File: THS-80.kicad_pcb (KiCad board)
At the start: 4 copper layers, 102.6 x 51.4 mm, 93 parts, among them J1 RC80 Bus, J2 CTC Header, J3 AVR-JTAG-10, J4 IDE, J5 PIO Header, J6 Port A, J7 Port B, J8 USB_B_Micro, Q1 IRLML6402, SW1 Reset, U1 DS1813R-5+T&R, U10 Z84C2010AEG, U11 74HCT273, U12 MAX40200AUK, U3 CPU -Z84C0020AEG, U4 CTC - Z84C3010AEG, U5 CPLD - EPM7032STC44, U6 SRAM - IS62C5128BL-45TLI, U7 74HCT2G04, U8 SST39SF040, U9 SIO/3 - Z84C4310AEG, X1 CFPS-72 50mhz

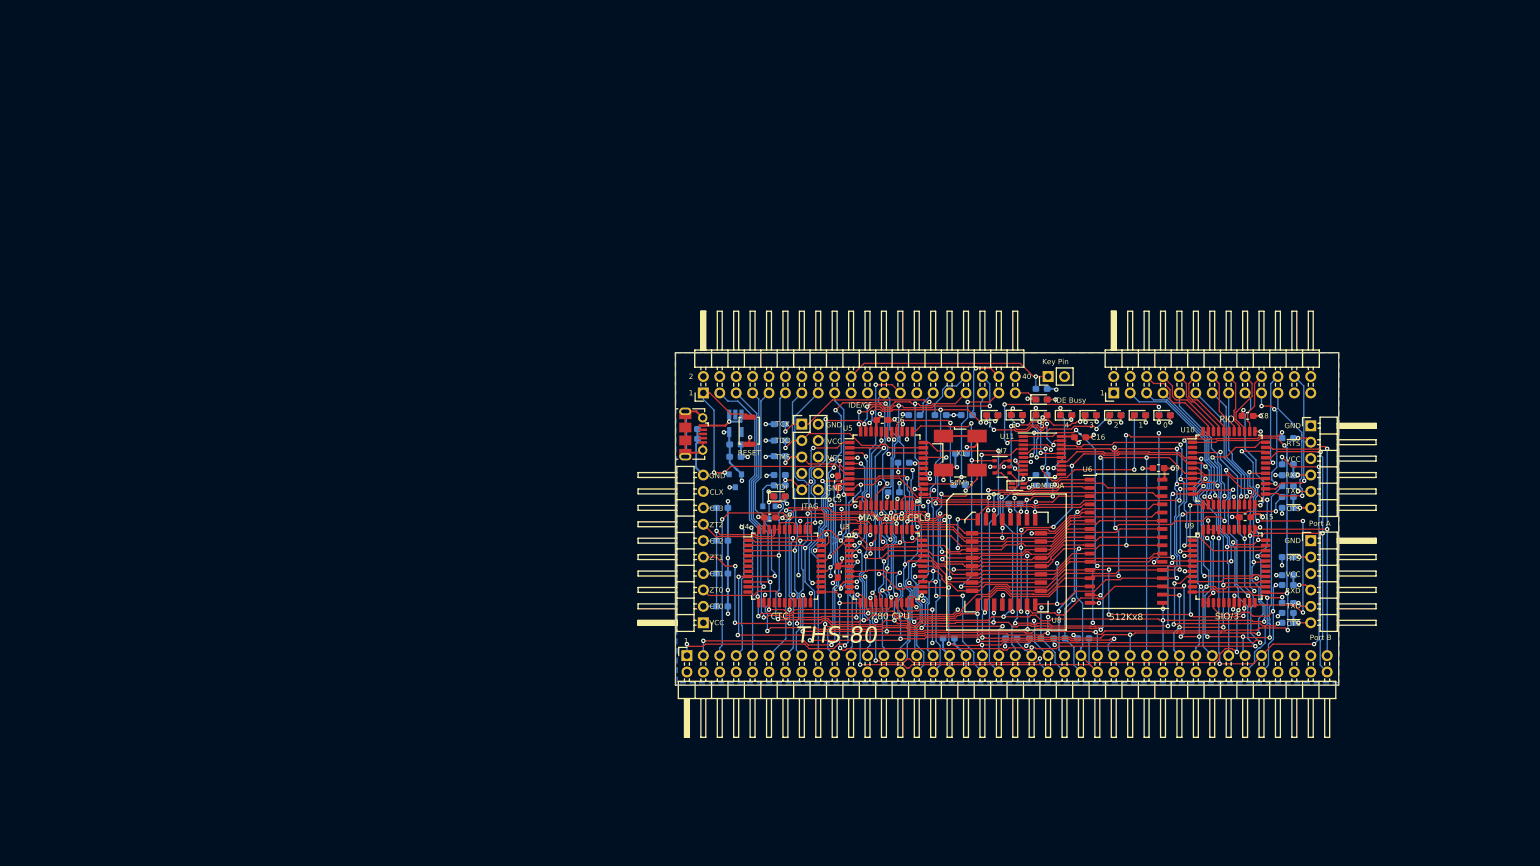
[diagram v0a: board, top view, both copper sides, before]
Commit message: connected sheet pins to bus
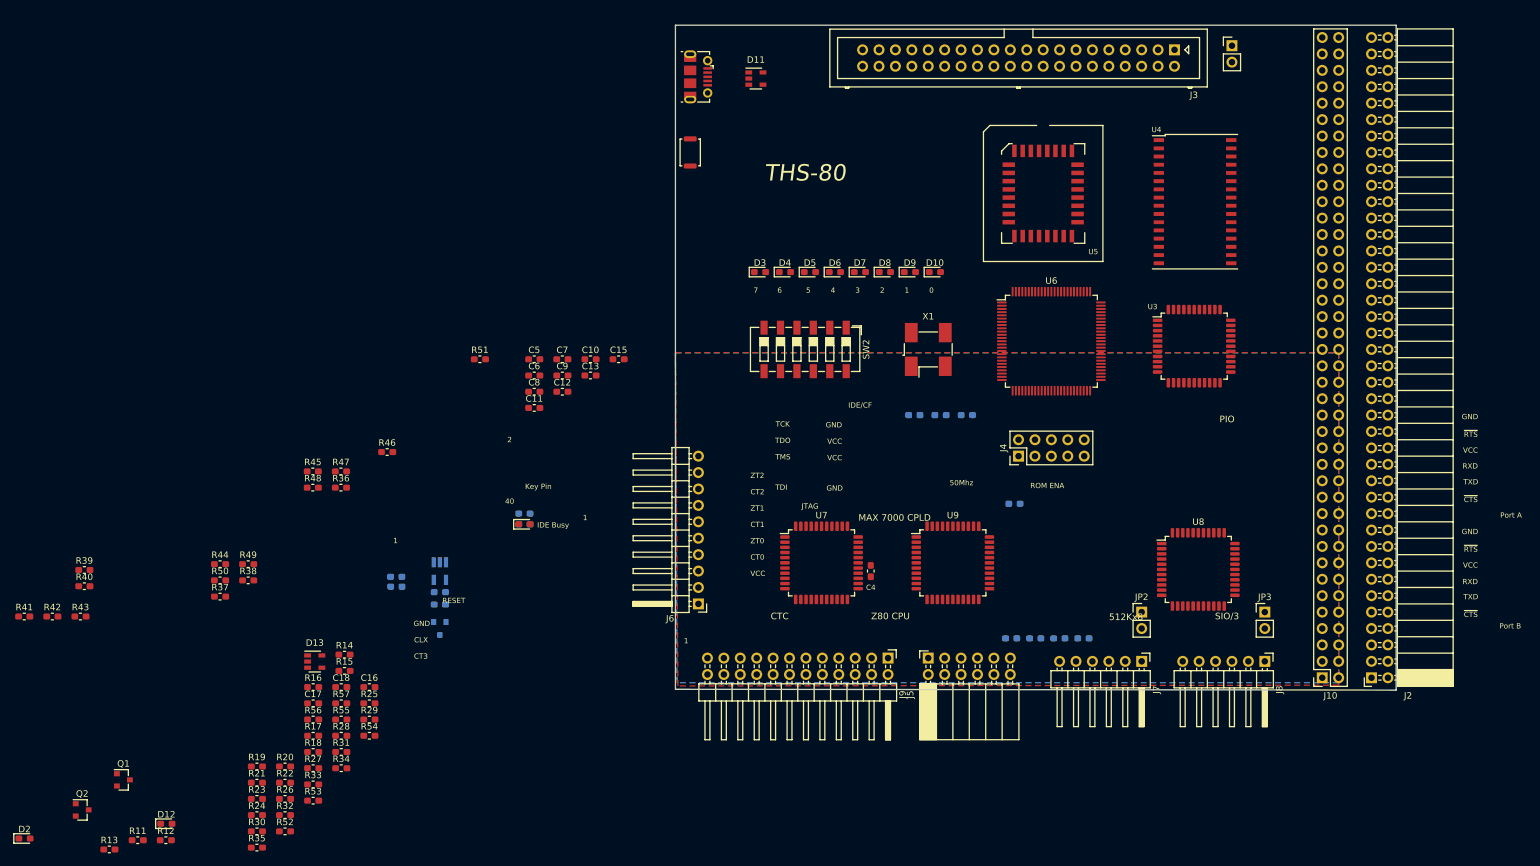
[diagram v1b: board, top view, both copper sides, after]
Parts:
- removed the C2 at (116.5, 107.3)
- removed the C3 at (137.2, 98.8)
- removed the C4 at (135.6, 103.4)
- removed the D1 at (117.9, 104.0)
- removed the J2 at (106.2, 123.6)
- removed the J3 at (121.4, 92.8)
- removed the R10 at (118.0, 92.8)
- removed the R3 at (145.8, 102.2)
- removed the R6 at (109.1, 116.0)
- removed the R7 at (109.1, 110.9)
- removed the R8 at (109.1, 105.8)
- removed the R9 at (109.1, 121.0)
- removed U10: Z84C2010AEG, Package_QFP:LQFP-44_10x10mm_P0.8mm
- removed U11: 74HCT273, Package_SO:TSSOP-20_4.4x6.5mm_P0.65mm
- removed the U4 at (118.7, 114.8)
- removed the U5 at (134.5, 99.7)
- added C10: 100nF, Capacitor_SMD:C_0603_1608Metric_Pad1.05x0.95mm_HandSolder, F.Cu at (88.7, 82.8)
- added C12: 100nF, Capacitor_SMD:C_0603_1608Metric_Pad1.05x0.95mm_HandSolder, F.Cu at (84.4, 87.8)
- added C13: 100nF, Capacitor_SMD:C_0603_1608Metric_Pad1.05x0.95mm_HandSolder, F.Cu at (88.7, 85.3)
- added C17: 100nF, Capacitor_SMD:C_0603_1608Metric_Pad1.05x0.95mm_HandSolder, F.Cu at (45.8, 136.0)
- added C18: 100nF, Capacitor_SMD:C_0603_1608Metric_Pad1.05x0.95mm_HandSolder, F.Cu at (50.1, 133.5)
- added D12: Green, LED_SMD:LED_0603_1608Metric_Pad1.05x0.95mm_HandSolder, F.Cu at (23.1, 154.7)
- added D13: SP0504BAHT, Package_TO_SOT_SMD:SOT-23-5, F.Cu at (46.0, 129.6)
- added D2: Green, LED_SMD:LED_0603_1608Metric_Pad1.05x0.95mm_HandSolder, F.Cu at (1.15, 156.9)
- added J10: RC80 Bus, Connector_PinSocket_2.54mm:PinSocket_2x40_P2.54mm_Vertical, F.Cu at (201.9, 132.1)
- added J4: JTAG, Connector_PinHeader_2.54mm:PinHeader_2x05_P2.54mm_Vertical, F.Cu at (154.9, 97.8)
- added J8: Port A, Connector_PinHeader_2.54mm:PinHeader_1x06_P2.54mm_Horizontal, F.Cu at (193.0, 129.5)
- added J9: PIO Header, Connector_PinHeader_2.54mm:PinHeader_2x12_P2.54mm_Horizontal, F.Cu at (134.7, 129.0)
- added JP2: 5V, Connector_PinHeader_2.54mm:PinHeader_1x02_P2.54mm_Vertical, F.Cu at (174.0, 121.9)
- added JP3: 5V, Connector_PinHeader_2.54mm:PinHeader_1x02_P2.54mm_Vertical, F.Cu at (193.0, 121.9)
- added Q2: IRLML6402, Package_TO_SOT_SMD:SOT-23, F.Cu at (10.1, 152.5)
- added R11: 100R, Resistor_SMD:R_0603_1608Metric_Pad1.05x0.95mm_HandSolder, F.Cu at (18.7, 157.2)
- added R16: 10K, Resistor_SMD:R_0603_1608Metric_Pad1.05x0.95mm_HandSolder, F.Cu at (45.8, 133.5)
- added R18: 200R, Resistor_SMD:R_0603_1608Metric_Pad1.05x0.95mm_HandSolder, F.Cu at (45.8, 143.6)
- added R21: 200R, Resistor_SMD:R_0603_1608Metric_Pad1.05x0.95mm_HandSolder, F.Cu at (37.1, 148.3)
- added R22: 680R, Resistor_SMD:R_0603_1608Metric_Pad1.05x0.95mm_HandSolder, F.Cu at (41.5, 148.3)
- added R43: 2K2, Resistor_SMD:R_0603_1608Metric_Pad1.05x0.95mm_HandSolder, F.Cu at (9.80, 122.6)
- added R44: 2K2, Resistor_SMD:R_0603_1608Metric_Pad1.05x0.95mm_HandSolder, F.Cu at (31.4, 114.5)
- added R45: 2K2, Resistor_SMD:R_0603_1608Metric_Pad1.05x0.95mm_HandSolder, F.Cu at (45.8, 100.2)
- added R46: 2K2, Resistor_SMD:R_0603_1608Metric_Pad1.05x0.95mm_HandSolder, F.Cu at (57.2, 97.2)
- added R47: 2K2, Resistor_SMD:R_0603_1608Metric_Pad1.05x0.95mm_HandSolder, F.Cu at (50.1, 100.2)
- added R48: 100K, Resistor_SMD:R_0603_1608Metric_Pad1.05x0.95mm_HandSolder, F.Cu at (45.8, 102.7)
- added R49: 100K, Resistor_SMD:R_0603_1608Metric_Pad1.05x0.95mm_HandSolder, F.Cu at (35.8, 114.5)
- added R50: 100K, Resistor_SMD:R_0603_1608Metric_Pad1.05x0.95mm_HandSolder, F.Cu at (31.4, 117.0)
- added R51: 100K, Resistor_SMD:R_0603_1608Metric_Pad1.05x0.95mm_HandSolder, F.Cu at (71.6, 82.8)
- added R52: 10K, Resistor_SMD:R_0603_1608Metric_Pad1.05x0.95mm_HandSolder, F.Cu at (41.5, 155.8)
- added R53: 10K, Resistor_SMD:R_0603_1608Metric_Pad1.05x0.95mm_HandSolder, F.Cu at (45.8, 151.1)
- added R54: 10K, Resistor_SMD:R_0603_1608Metric_Pad1.05x0.95mm_HandSolder, F.Cu at (54.5, 141.1)
- added R55: 10K, Resistor_SMD:R_0603_1608Metric_Pad1.05x0.95mm_HandSolder, F.Cu at (50.1, 138.5)
- added R56: 10K, Resistor_SMD:R_0603_1608Metric_Pad1.05x0.95mm_HandSolder, F.Cu at (45.8, 138.5)
- added R57: 10K, Resistor_SMD:R_0603_1608Metric_Pad1.05x0.95mm_HandSolder, F.Cu at (50.1, 136.0)
- added SW2: SW_DIP_x06, Button_Switch_SMD:SW_DIP_SPSTx06_Slide_6.7x16.8mm_W6.73mm_P2.54mm_LowProfile_JPin, F.Cu at (121.9, 81.3)
- added U6: EPM7064STC100, Package_QFP:TQFP-100_14x14mm_P0.5mm, F.Cu at (160.0, 80.0)
- added U8: SIO/3 - Z84C4310AEG, Package_QFP:LQFP-44_10x10mm_P0.8mm, F.Cu at (182.8, 115.3)
- C11, Q1, R15, R17, R23, R24, R25, R26, R27, R28, R29: moved to F.Cu
- C16: value 100nF -> 2.2uF
- C7: value 2.2uF -> 100nF; moved to F.Cu
- D11: value Green -> SP0504BAHT; footprint LED_SMD:LED_0603_1608Metric_Pad1.05x0.95mm_HandSolder -> Package_TO_SOT_SMD:SOT-23-5
- D3: value Red/Green -> Green; footprint LED_SMD:LED_2C_0603_1608Metric_Pad1.05x0.95mm_HandSolder -> LED_SMD:LED_0603_1608Metric_Pad1.05x0.95mm_HandSolder
- J2: renamed from J1; footprint Connector_PinHeader_2.54mm:PinHeader_2x40_Top_Bottom_P2.54mm_Horizontal -> Connector_PinSocket_2.54mm:PinSocket_2x40_P2.54mm_Horizontal
- J3: renamed from J4; footprint Connector_PinHeader_2.54mm:PinHeader_2x20_P2.54mm_Horizontal -> Connector_Multicomp:Multicomp_MC9A12-4034_2x20_P2.54mm_Vertical
- J5: value PIO Header -> PMOD; footprint Connector_PinHeader_2.54mm:PinHeader_2x13_P2.54mm_Horizontal -> Connector_PinSocket_2.54mm:PinSocket_2x06_P2.54mm_Horizontal
- J6: value Port A -> CTC Header; footprint Connector_PinHeader_2.54mm:PinHeader_1x06_P2.54mm_Horizontal -> Connector_PinHeader_2.54mm:PinHeader_1x10_P2.54mm_Horizontal
- JP1: value Jumper_NC_Small -> Keypin
- R12: value 10K -> 1K; moved to F.Cu
- R13: value 100R -> 10K; moved to F.Cu
- R14: value 10K -> 100R; moved to F.Cu
- R19, R20: value 680R -> 200R; moved to F.Cu
- R30: value 680R -> 100R; moved to F.Cu
- R31: value 2K2 -> 360R; moved to F.Cu
- R32, R33, R34, R35: value 2K2 -> 200R; moved to F.Cu
- R36, R37, R38: value 2K2 -> 10K; moved to F.Cu
- R39: value 100K -> 10K; moved to F.Cu
- R40, R41, R42: value 100K -> 2K2; moved to F.Cu
- U7: value 74HCT2G04 -> CTC - Z84C3010AEG; footprint Package_SO:TSOP-6_1.65x3.05mm_P0.95mm -> Package_QFP:LQFP-44_10x10mm_P0.8mm
- U9: value SIO/3 - Z84C4310AEG -> Z84C2010AEG
- moved R41 196.2 mm to (1.10, 122.6), turned to 0 degrees
- moved R42 191.1 mm to (5.45, 122.6), turned to 0 degrees
- moved R39 186.8 mm to (10.4, 115.4)
- moved R40 186.2 mm to (10.4, 117.9)
- moved R35 165.7 mm to (37.1, 158.4), turned to 0 degrees
- moved R37 165.2 mm to (31.4, 119.5), turned to 0 degrees
- moved R32 164.4 mm to (41.5, 153.3), turned to 0 degrees
- moved R38 161.0 mm to (35.8, 117.0), turned to 0 degrees
- moved R33 157.7 mm to (45.8, 148.6), turned to 0 degrees
- moved R31 154.3 mm to (50.1, 143.6), turned to 0 degrees
- moved R23 152.5 mm to (37.1, 150.8)
- moved R34 152.3 mm to (50.1, 146.1), turned to 0 degrees
- moved R24 150.0 mm to (37.1, 153.3)
- moved R36 147.3 mm to (50.1, 102.7), turned to 0 degrees
- moved R26 138.1 mm to (41.5, 150.8)
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- renumbered C12 to C1, C10 to C14, C14 to C2, C13 to C3, C1 to C4, D2 to D1, J8 to J1, R43 to R1, R11 to R10, R1 to R2, R2 to R3, R16 to R6, R18 to R7, R21 to R8, R22 to R9, U12 to U2, U6 to U4, U8 to U5
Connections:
- D10 pad 1: GND -> /CPLD/LED7
- D11 pad 1: GND -> Net-(D11-Pad1)
- D11 pad 2: Net-(D11-Pad2) -> GND
- D3 pad 1: Net-(D3-Pad1) -> /CPLD/LED0
- D4 pad 1: GND -> /CPLD/LED1
- D5 pad 1: GND -> /CPLD/LED2
- D6 pad 1: GND -> /CPLD/LED3
- D7 pad 1: GND -> /CPLD/LED4
- D8 pad 1: GND -> /CPLD/LED5
- D9 pad 1: GND -> /CPLD/LED6
- J1 pad 2: Net-(J8-Pad2) -> (no net)
- J1 pad 3: Net-(J8-Pad3) -> (no net)
- J1 pad 4: Net-(J8-Pad4) -> (no net)
- J2 pad 10: /A6 -> (no net)
- J2 pad 11: /A5 -> /A10
- J2 pad 12: /A4 -> (no net)
- J2 pad 13: /A3 -> /A9
- J2 pad 14: /A2 -> (no net)
- J2 pad 15: /A1 -> /A8
- J2 pad 16: /A0 -> (no net)
- J2 pad 17: GND -> /A7
- J2 pad 18: VCC -> /A23
- J2 pad 19: /~M1 -> /A6
- J2 pad 2: /A14 -> (no net)
- J2 pad 20: /~RESET -> /A22
- J2 pad 21: /CLK_CPU -> /A5
- J2 pad 22: /~INT -> /A21
- J2 pad 23: /~MREQ -> /A4
- J2 pad 24: /~WR -> /A20
- J2 pad 25: /~RD -> /A3
- J2 pad 26: /~IORQ -> /A19
- J2 pad 27: /D0 -> /A2
- J2 pad 28: /D1 -> /A18
- J2 pad 29: /D2 -> /A1
- J2 pad 3: /A13 -> /A14
- J2 pad 30: /D3 -> /A17
- J2 pad 31: /D4 -> /A0
- J2 pad 32: /D5 -> /A16
- J2 pad 33: /D6 -> GND
- J2 pad 34: /D7 -> GND
- J2 pad 35: /TXA -> VCC
- J2 pad 36: /RXA -> VCC
- J2 pad 37: /USR1 -> /~M1
- J2 pad 38: /USR2 -> /~RFSH
- J2 pad 39: /USR3 -> /~RESET
- J2 pad 4: /A12 -> (no net)
- J2 pad 40: /IEI -> /~PAGE
- J2 pad 41: Net-(J1-Pad41) -> /CLK_CPU
- J2 pad 42: Net-(J1-Pad42) -> /CLK2
- J2 pad 43: Net-(J1-Pad43) -> /~INT
- J2 pad 44: Net-(J1-Pad44) -> /~BUSACK
- J2 pad 45: Net-(J1-Pad45) -> /~MREQ
- J2 pad 46: Net-(J1-Pad46) -> /~HALT
- J2 pad 47: Net-(J1-Pad47) -> /~WR
- J2 pad 48: Net-(J1-Pad48) -> /~BUSREQ
- J2 pad 49: /A23 -> /~RD
- J2 pad 5: /A11 -> /A13
- J2 pad 50: /A22 -> /~WAIT
- J2 pad 51: /A21 -> /~IORQ
- J2 pad 52: /A20 -> /~NMI
- J2 pad 53: /A19 -> /D0
- J2 pad 54: /A18 -> /D8
- J2 pad 55: /A17 -> /D1
- J2 pad 56: /A16 -> /D9
- J2 pad 57: GND -> /D2
- J2 pad 58: VCC -> /D10
- J2 pad 59: /~RFSH -> /D3
- J2 pad 6: /A10 -> (no net)
- J2 pad 60: /~PAGE -> /D11
- J2 pad 61: /CLK2 -> /D4
- J2 pad 62: /~BUSACK -> /D12
- J2 pad 63: /~HALT -> /D5
- J2 pad 64: /~BUSREQ -> /D13
- J2 pad 65: /~WAIT -> /D6
- J2 pad 66: /~NMI -> /D14
- J2 pad 67: /D8 -> /D7
- J2 pad 68: /D9 -> /D15
- J2 pad 69: /D10 -> /TXA
- J2 pad 7: /A9 -> /A12
- J2 pad 70: /D11 -> /TXB
- J2 pad 71: /D12 -> /RXA
- J2 pad 72: /D13 -> /RXB
- J2 pad 73: /D14 -> /USR1
- J2 pad 74: /D15 -> /USR5
- J2 pad 75: /TXB -> /USR2
- J2 pad 76: /RXB -> /USR6
- J2 pad 77: /USR5 -> /USR3
- J2 pad 78: /USR6 -> /USR7
- J2 pad 79: /USR7 -> /IEI
- J2 pad 8: /A8 -> (no net)
- J2 pad 9: /A7 -> /A11
- J3 pad 10: Net-(J4-Pad10) -> (no net)
- J3 pad 12: Net-(J4-Pad12) -> (no net)
- J3 pad 14: Net-(J4-Pad14) -> (no net)
- J3 pad 16: Net-(J4-Pad16) -> (no net)
- J3 pad 18: Net-(J4-Pad18) -> (no net)
- J3 pad 21: Net-(J4-Pad21) -> (no net)
- J3 pad 27: Net-(J4-Pad27) -> (no net)
- J3 pad 28: Net-(J4-Pad28) -> (no net)
- J3 pad 31: Net-(J4-Pad31) -> (no net)
- J3 pad 32: Net-(J4-Pad32) -> (no net)
- J3 pad 4: Net-(J4-Pad4) -> (no net)
- J3 pad 6: Net-(J4-Pad6) -> (no net)
- J3 pad 8: Net-(J4-Pad8) -> (no net)
- J5 pad 1: VCC -> Net-(D11-Pad1)
- J5 pad 10: /PB5 -> Net-(D13-Pad5)
- J5 pad 11: /PA3 -> GND
- J5 pad 12: /PB4 -> VCC
- J5 pad 2: GND -> Net-(D11-Pad3)
- J5 pad 3: /PA7 -> Net-(D11-Pad4)
- J5 pad 4: GND -> Net-(D11-Pad5)
- J5 pad 5: /PA6 -> GND
- J5 pad 6: /PB7 -> VCC
- J5 pad 7: /PA5 -> Net-(D13-Pad1)
- J5 pad 8: /PB6 -> Net-(D13-Pad3)
- J5 pad 9: /PA4 -> Net-(D13-Pad4)
- J6 pad 1: GND -> VCC
- J6 pad 2: Net-(J6-Pad2) -> /CLK_U
- J6 pad 3: Net-(J6-Pad3) -> /Peripherals/ZT0
- J6 pad 4: Net-(J6-Pad4) -> /CLK_U
- J6 pad 5: Net-(J6-Pad5) -> /Peripherals/ZT1
- J6 pad 6: Net-(J6-Pad6) -> /CLK_U
- R12 pad 1: VCC -> GND
- R12 pad 2: /TMS -> /CPLD/TCK
- R13 pad 1: Net-(Q1-Pad1) -> VCC
- R13 pad 2: /TDI -> /CPLD/TMS
- R14 pad 1: VCC -> Net-(Q1-Pad1)
- R14 pad 2: /TDO -> /CPLD/TDI
- R15 pad 2: /TDI -> /CPLD/TDO
- R19 pad 1: Net-(D3-Pad1) -> Net-(D11-Pad3)
- R19 pad 2: VCC -> /CPLD/PMOD1
- R20 pad 1: Net-(D3-Pad3) -> Net-(D11-Pad4)
- R20 pad 2: VCC -> /CPLD/PMOD2
- R23 pad 1: Net-(R23-Pad1) -> VCC
- R24 pad 1: Net-(R24-Pad1) -> VCC
- R25 pad 1: Net-(R25-Pad1) -> VCC
- R26 pad 1: Net-(R26-Pad1) -> VCC
- R27 pad 1: Net-(R27-Pad1) -> VCC
- R28 pad 1: Net-(R28-Pad1) -> VCC
- R29 pad 1: Net-(R29-Pad1) -> VCC
- R30 pad 2: Net-(D11-Pad2) -> /~PAGE
- R31 pad 1: Net-(J6-Pad2) -> Net-(D12-Pad1)
- R31 pad 2: /~RTSA -> GND
- R32 pad 1: Net-(J6-Pad4) -> Net-(D13-Pad1)
- R32 pad 2: /RXA -> /CPLD/PMOD4
- R33 pad 1: Net-(J6-Pad5) -> Net-(D13-Pad3)
- R33 pad 2: /TXA -> /CPLD/PMOD5
- R34 pad 1: Net-(J6-Pad6) -> Net-(D13-Pad4)
- R34 pad 2: /~CTSA -> /CPLD/PMOD6
- R35 pad 1: Net-(J7-Pad2) -> Net-(D13-Pad5)
- R35 pad 2: /~RTSB -> /CPLD/PMOD7
- R36 pad 1: Net-(J7-Pad4) -> VCC
- R36 pad 2: /RXB -> /CLK_U
- R37 pad 1: Net-(J7-Pad5) -> VCC
- R37 pad 2: /TXB -> /CLK_U
- R38 pad 1: Net-(J7-Pad6) -> VCC
- R38 pad 2: /~CTSB -> /CLK_U
- R39 pad 2: Net-(J6-Pad4) -> /CLK_U
- R40 pad 1: VCC -> Net-(J7-Pad2)
- R40 pad 2: Net-(J7-Pad4) -> /Peripherals/~RTSB
- R41 pad 1: Net-(J6-Pad6) -> Net-(J7-Pad4)
- R41 pad 2: GND -> /Peripherals/RXB
- R42 pad 1: Net-(J7-Pad6) -> Net-(J7-Pad5)
- R42 pad 2: GND -> /Peripherals/TXB
- U2 pad 4: Net-(U12-Pad4) -> (no net)
- U3 pad 11: Net-(U3-Pad11) -> (no net)
- U3 pad 17: Net-(U3-Pad17) -> (no net)
- U3 pad 33: Net-(U3-Pad33) -> (no net)
- U3 pad 39: Net-(U3-Pad39) -> (no net)
- U7 pad 1: /ROM_~CE~ -> /Peripherals/A0
- U7 pad 2: GND -> /Peripherals/A1
- U7 pad 3: Net-(D3-Pad2) -> /Peripherals/D2
- U7 pad 4: Net-(D3-Pad4) -> /Peripherals/D3
- U7 pad 5: VCC -> (no net)
- U7 pad 6: Net-(D3-Pad2) -> (no net)
- U9 pad 1: Net-(U9-Pad1) -> /~IORQ
- U9 pad 10: Net-(U9-Pad10) -> /PIO_~CE
- U9 pad 11: /TXB -> /Peripherals/A1
- U9 pad 12: /CLK_UART -> /Peripherals/A0
- U9 pad 13: /CLK_UART -> /Peripherals/PA7
- U9 pad 14: /RXB -> /Peripherals/PA6
- U9 pad 15: Net-(U9-Pad15) -> /Peripherals/PA5
- U9 pad 16: Net-(U9-Pad16) -> /Peripherals/PA4
- U9 pad 17: Net-(U9-Pad17) -> (no net)
- U9 pad 19: /~RD -> /Peripherals/PA3
- U9 pad 2: /~RTSA -> (no net)
- U9 pad 20: /A0 -> /Peripherals/PA2
- U9 pad 21: /A1 -> /Peripherals/PA1
- U9 pad 22: /SIO_~CE~ -> /Peripherals/PA0
- U9 pad 23: /~IORQ -> /Peripherals/~ASTB
- U9 pad 24: /D6 -> /Peripherals/~BSTB
- U9 pad 25: /D4 -> /Peripherals/ARDY
- U9 pad 26: /D2 -> /Peripherals/A0
- U9 pad 27: /DO -> /Peripherals/A1
- U9 pad 28: Net-(U9-Pad28) -> (no net)
- U9 pad 29: /D1 -> /Peripherals/BRDY
- U9 pad 3: /~CTSA -> /~M1
- U9 pad 30: /D3 -> /Peripherals/IEO
- U9 pad 31: /D5 -> /Peripherals/IEI
- U9 pad 32: /D7 -> /~INT
- U9 pad 33: /~INT -> /CLK_CPU
- U9 pad 34: /IEI -> VCC
- U9 pad 35: /IEO -> /Peripherals/PB0
- U9 pad 36: /~M1 -> /Peripherals/PB1
- U9 pad 37: VCC -> /Peripherals/PB2
- U9 pad 38: Net-(U9-Pad38) -> /Peripherals/PB3
- U9 pad 39: Net-(U9-Pad39) -> (no net)
- U9 pad 4: GND -> /Peripherals/D5
- U9 pad 40: Net-(U9-Pad40) -> /Peripherals/PB4
- U9 pad 41: /RXA -> /Peripherals/PB5
- U9 pad 42: /CLK_UART -> /Peripherals/PB6
- U9 pad 43: /CLK_UART -> /Peripherals/PB7
- U9 pad 44: /TXA -> /~RD
- U9 pad 5: /CLK_CPU -> /Peripherals/D4
- U9 pad 6: /~RESET -> /Peripherals/D3
- U9 pad 7: GND -> /Peripherals/D2
- U9 pad 8: /~CTSB -> /Peripherals/D7
- U9 pad 9: /~RTSB -> /Peripherals/D6
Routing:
- net /D4: track 234.2 -> 0.00 mm, vias 16 -> 0
- net /D5: track 229.5 -> 0.00 mm, vias 12 -> 0
- net /D1: track 228.2 -> 0.00 mm, vias 12 -> 0
- net /D2: track 227.4 -> 0.00 mm, vias 13 -> 0
- net /D7: track 208.6 -> 0.00 mm, vias 10 -> 0
- net /D6: track 207.9 -> 0.00 mm, vias 11 -> 0
- net /D3: track 203.3 -> 0.00 mm, vias 12 -> 0
- net /~RESET: track 202.2 -> 0.00 mm, vias 14 -> 0
- net /D0: track 199.8 -> 0.00 mm, vias 15 -> 0
- net /~RD: track 191.6 -> 0.00 mm, vias 12 -> 0
- net /A0: track 177.4 -> 0.00 mm, vias 13 -> 0
- net /A1: track 170.9 -> 0.00 mm, vias 10 -> 0
- net /~IORQ: track 170.5 -> 0.00 mm, vias 10 -> 0
- net /CLK_CPU: track 139.5 -> 0.00 mm, vias 9 -> 0
- net /~M1: track 137.0 -> 0.00 mm, vias 10 -> 0
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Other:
- board size 102.6 x 51.4 mm -> 111.5 x 102.9 mm

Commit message: fixed up interrupt chain wiring
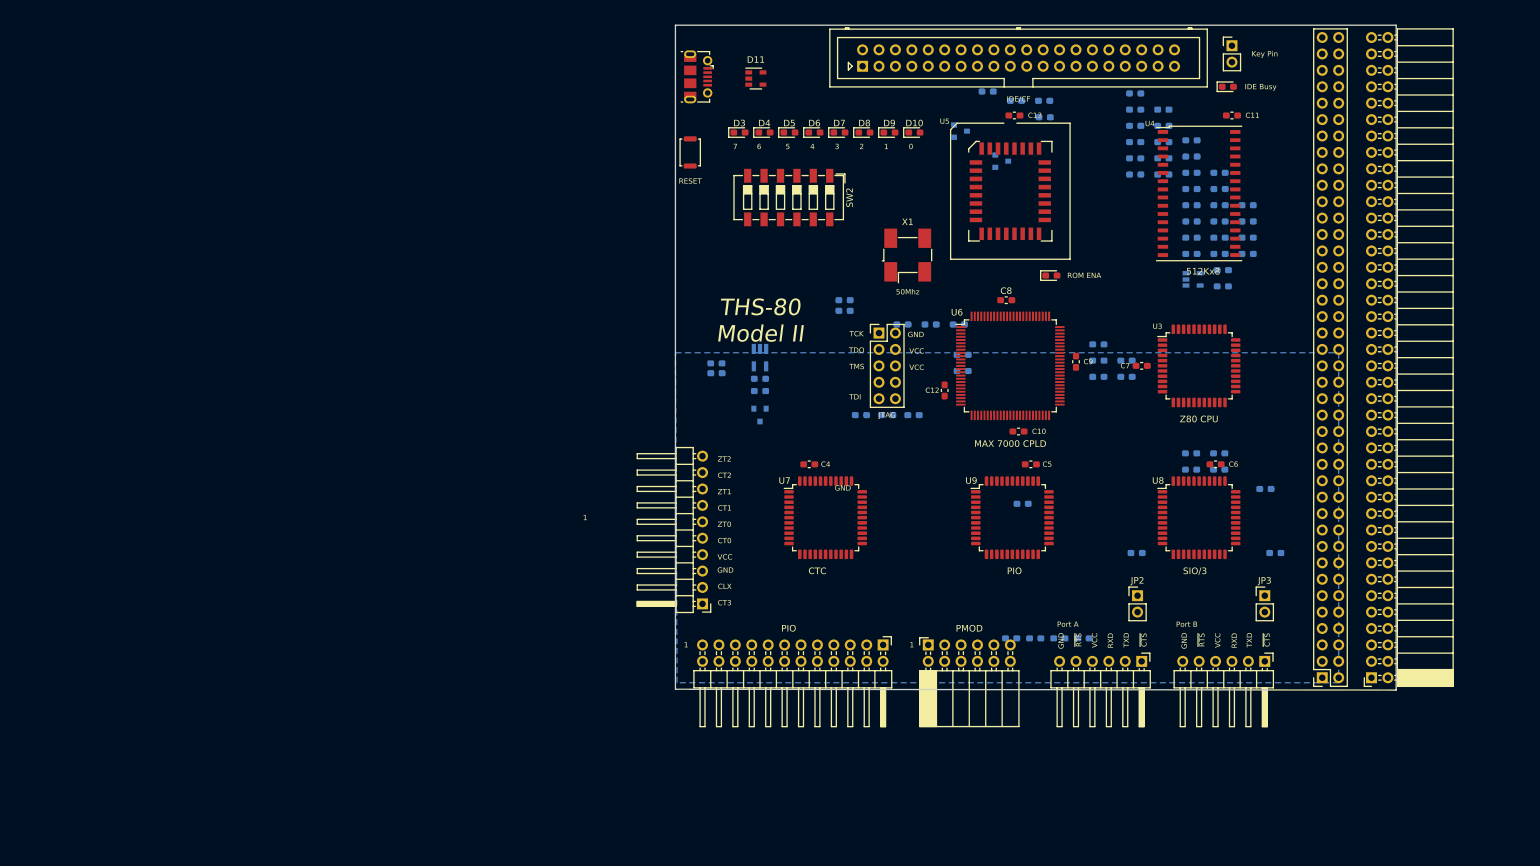
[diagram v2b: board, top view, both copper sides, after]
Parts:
- C15, C16, C17, C18, D12, D13, Q1, Q2, R11, R12, R13, R14, R15, R16, R17, R18, R19, R20, R21, R22, R23, R24, R25, R26, R27, R28, R29, R30, R31, R32, R33, R34, R35, R36, R37, R38, R39, R40, R41, R42, R43, R44, R45, R46, R47, R48, R49, R50, R51, R52, R53, R54, R55, R56, R57: moved to B.Cu
- moved D2 181.2 mm to (160.0, 69.8)
- moved R13 179.5 mm to (150.2, 41.4)
- moved R35 179.1 mm to (173.0, 41.7)
- moved R11 177.6 mm to (154.6, 42.8)
- moved R12 177.6 mm to (158.9, 42.8)
- moved R30 175.9 mm to (173.0, 44.2)
- moved R52 175.9 mm to (177.3, 44.2)
- moved D12 174.4 mm to (159.0, 45.4)
- moved R24 172.7 mm to (173.0, 46.7)
- moved R32 172.7 mm to (177.3, 46.7)
- moved Q2 171.7 mm to (146.0, 47.5)
- moved R53 170.0 mm to (181.7, 48.9)
- moved R23 169.7 mm to (173.0, 49.2)
- moved R26 169.7 mm to (177.3, 49.2)
- moved R33 167.0 mm to (181.7, 51.4)
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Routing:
- removed copper zone on F.Cu, net GND
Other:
- board text added: "PMOD"
- board text added: "THS-80 Model II"
- board text removed: "40"
- board text removed: "THS-80"
